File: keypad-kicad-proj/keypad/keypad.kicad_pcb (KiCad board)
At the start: 2 copper layers, 160 x 125 mm, 103 parts, among them J1 Screw_Terminal_01x02, J2 USB4105-GF-A, J3 USB4105-GF-A, J4 Micro_SD_Card_Det_Hirose_DM3AT, Q1 BC817, Q2 BC817, Q3 IRF9393TRPBF, SW1 RotaryEncoder, SW2 RotaryEncoder, SW25 SW_RST, SW26 Cherry_MX, SW27 Cherry_MX, SW28 Cherry_MX, SW32 Cherry_MX, SW33 Cherry_MX, SW34 Cherry_MX, SW38 Cherry_MX, SW39 Cherry_MX, SW40 Cherry_MX, SW44 Cherry_MX, SW45 Cherry_MX, SW46 Cherry_MX, U1 ESP32-S3-WROOM-1, U10 SK6812MINI-E, U11 SK6812MINI-E, U12 SK6812MINI-E, U13 SK6812MINI-E, U14 SK6812MINI-E, U2 TLV75901PDRVT, U27 SK6812MINI-E, U3 CP2102N-A01-GQFN24, U4 SK6812MINI-E, U5 SK6812MINI-E, U6 SK6812MINI-E, U7 SK6812MINI-E, U8 SK6812MINI-E, U9 SK6812MINI-E

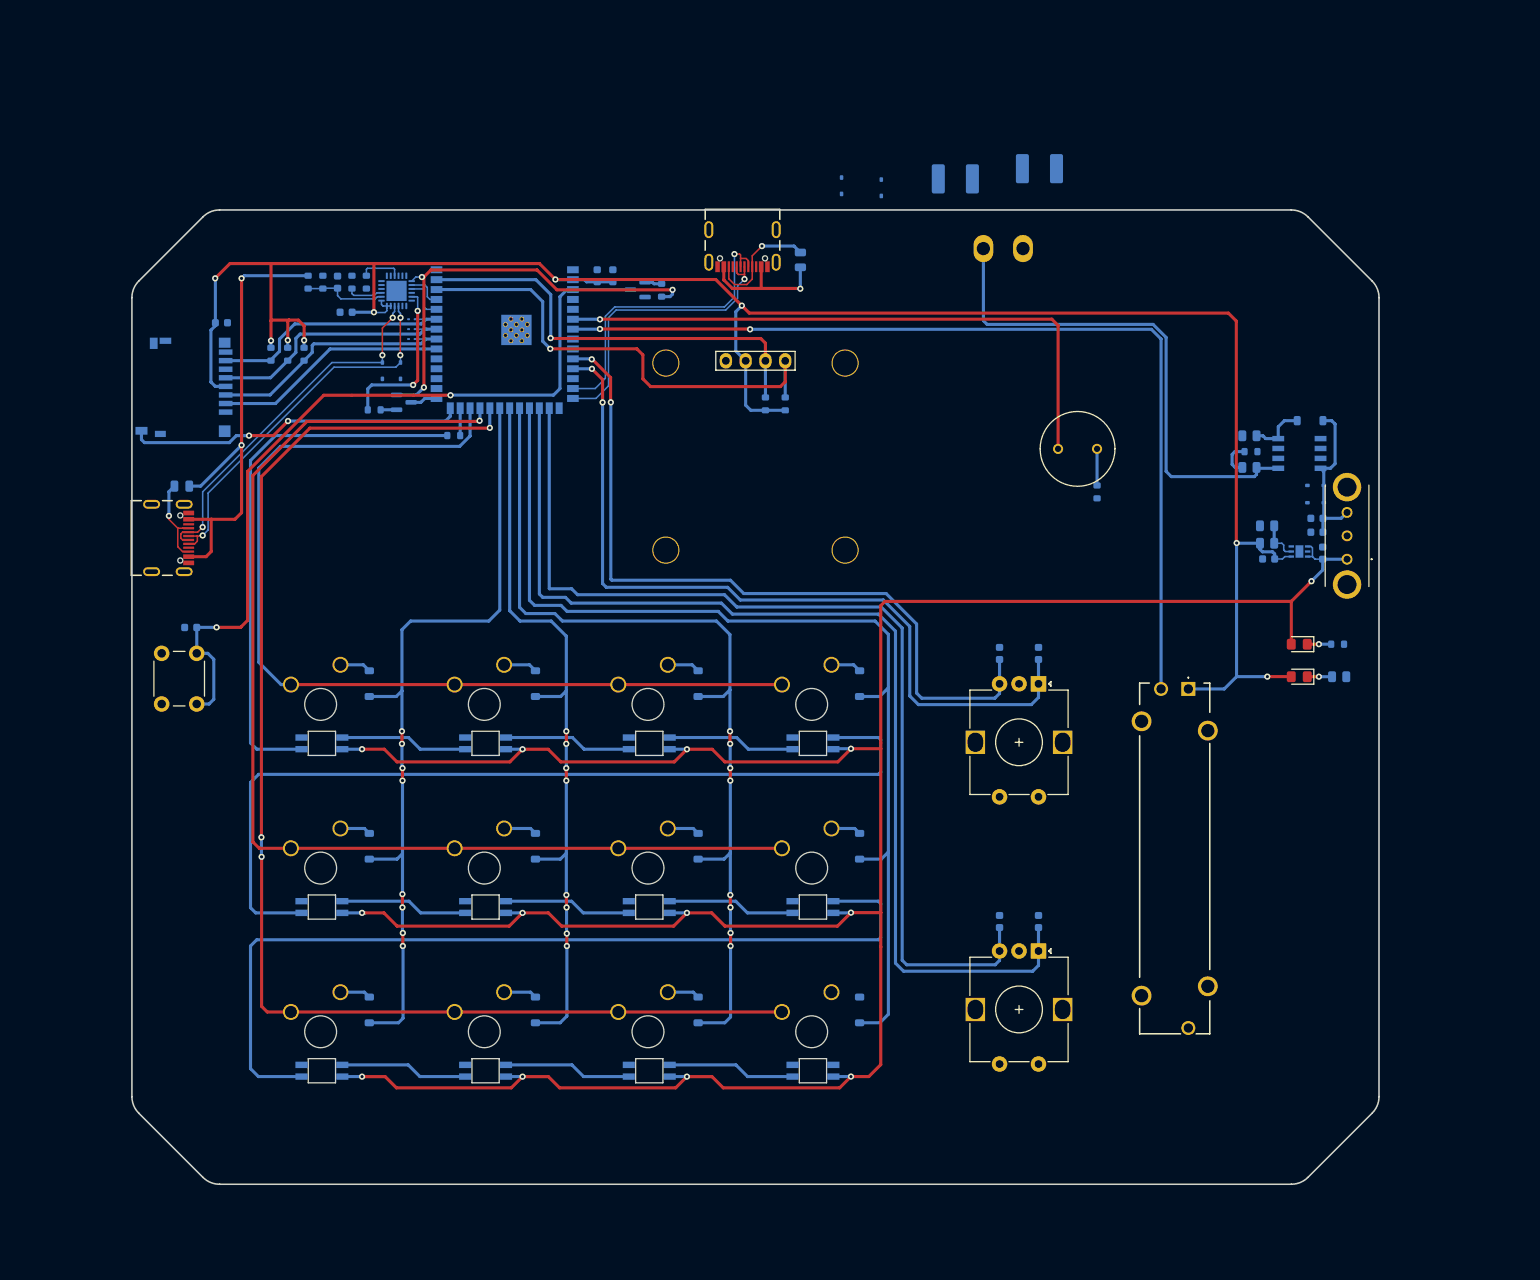
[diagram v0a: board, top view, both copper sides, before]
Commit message: assigned different pins so it's easier for the layout
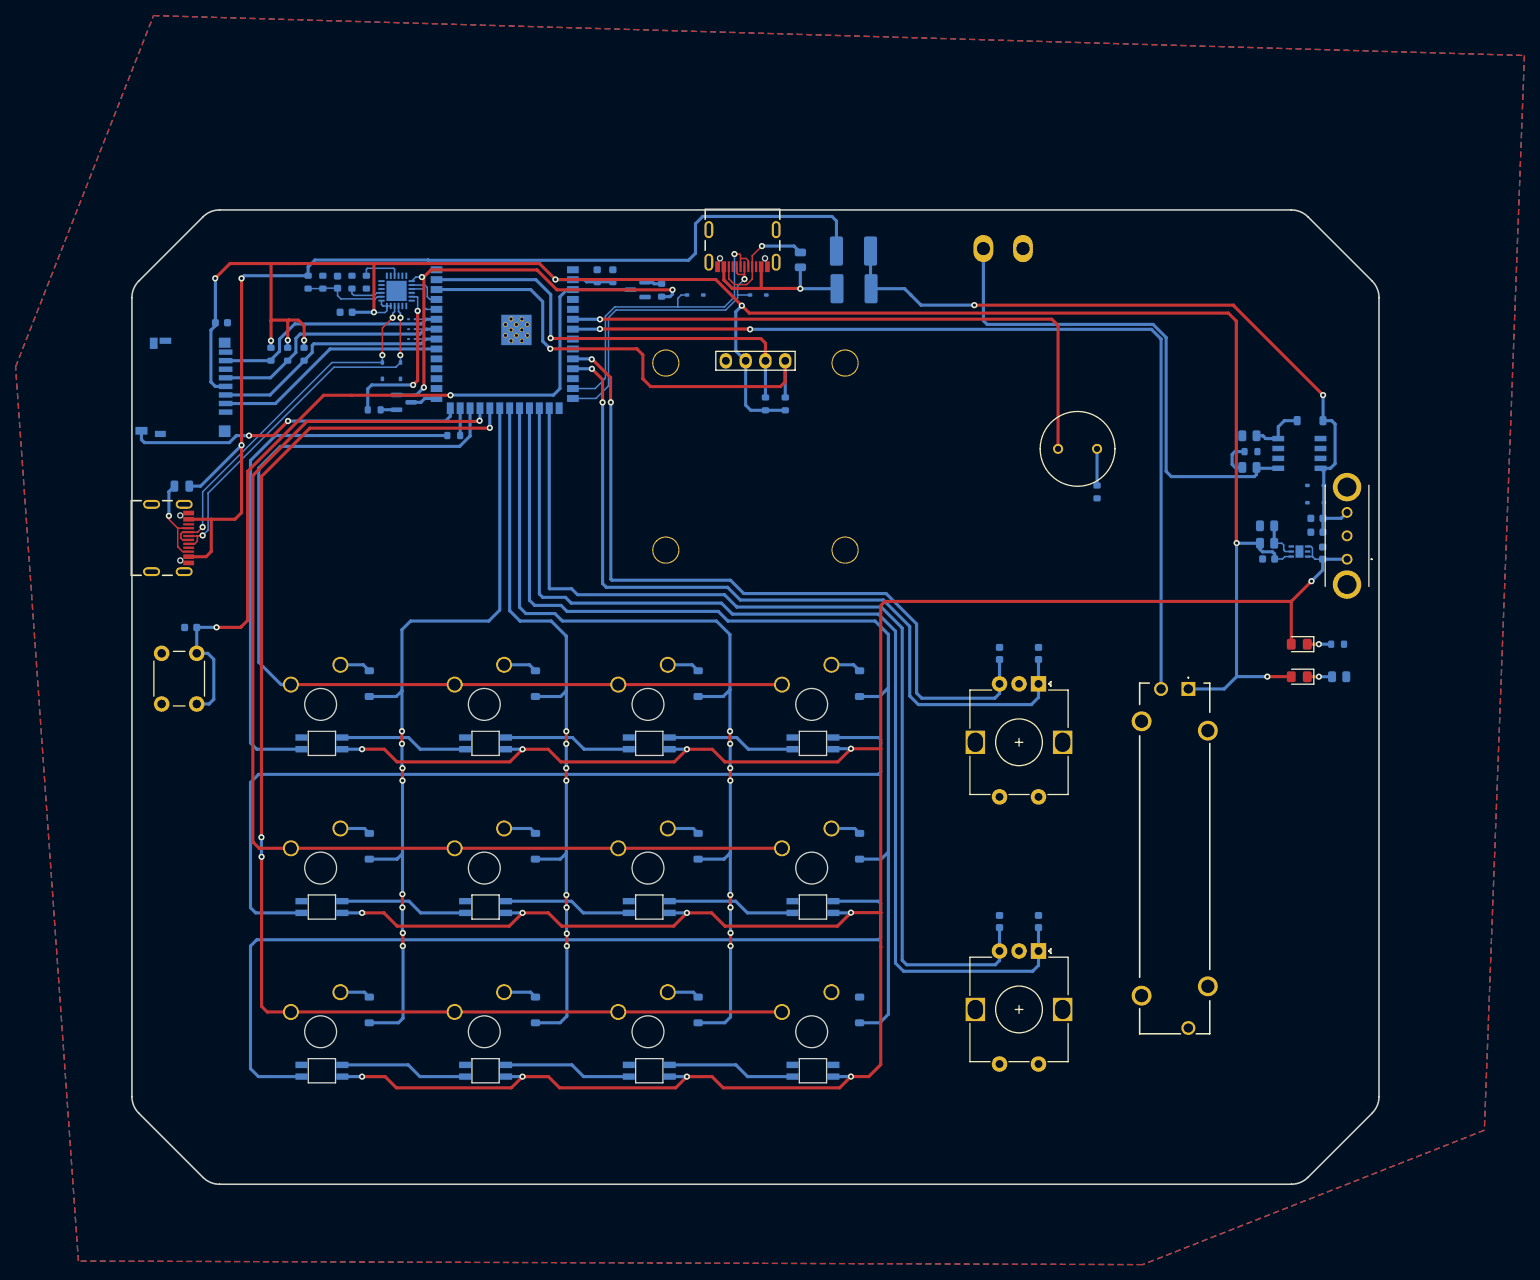
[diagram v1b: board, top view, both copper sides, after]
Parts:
- moved D16 27.6 mm to (121.8, 50.8), turned to 0 degrees
- moved D18 26.1 mm to (142.1, 45.1)
- moved D17 19.2 mm to (142.2, 50.0)
- moved D15 17.6 mm to (129.9, 50.8), turned to 0 degrees
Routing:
- net USB-C_UART_VBUS: track 62.1 -> 140.0 mm
- net USB-C_OTG_5V: track 20.8 -> 92.6 mm, vias 0 -> 2
- net Net-(D17-A): track 17.5 -> 22.2 mm
- net USB-C_OTG_D-: track 40.0 -> 42.4 mm
- net USB-C_OTG_D+: track 37.9 -> 39.5 mm
- added copper zone on B.Cu, net GND
- added copper zone on F.Cu, net GND
